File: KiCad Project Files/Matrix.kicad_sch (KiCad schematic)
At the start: 202 parts

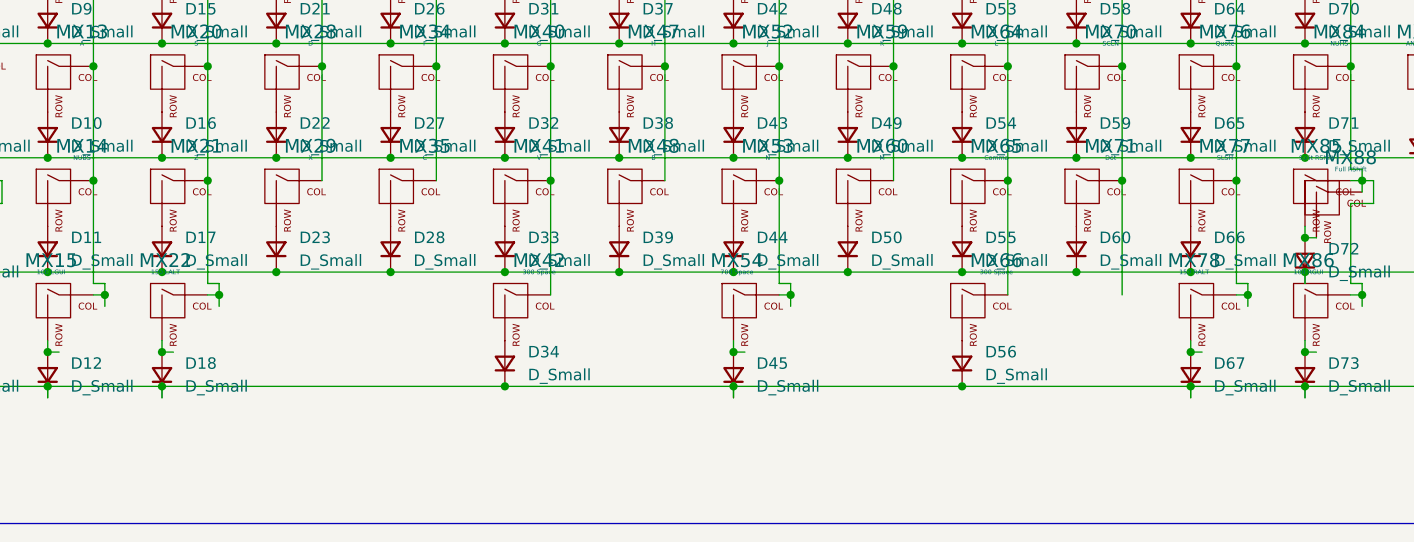
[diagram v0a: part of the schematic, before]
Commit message: added 225/275 support
2.75 stabs have break-away screw holes for compatibility with cases that need those areas of the PCB to be cut away
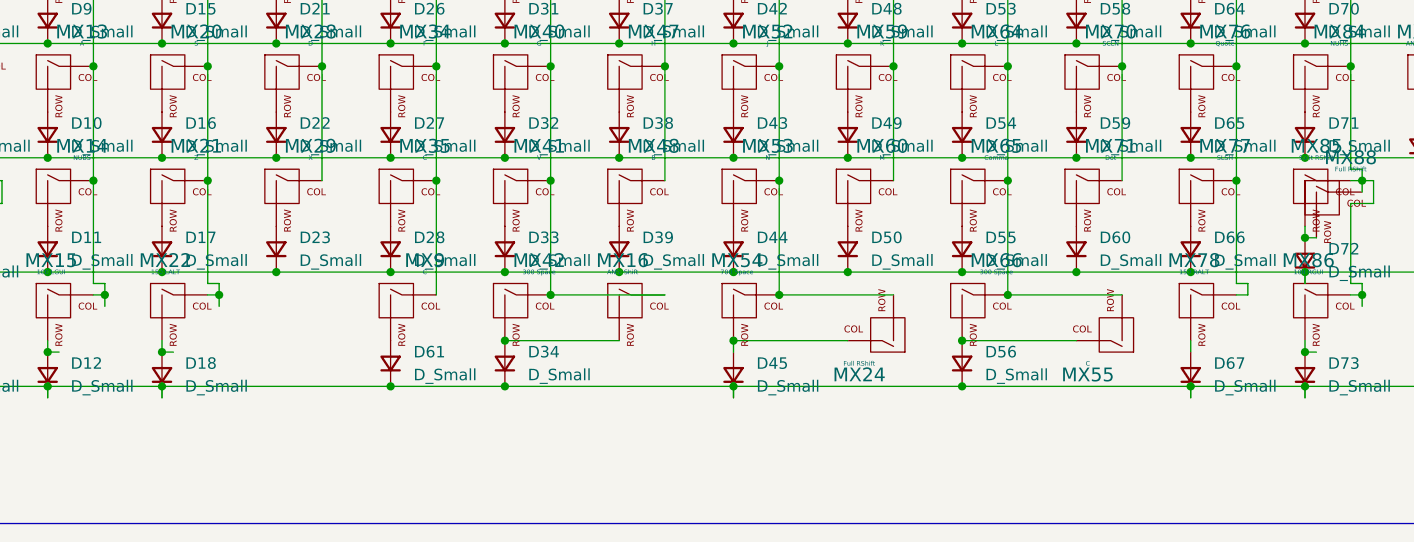
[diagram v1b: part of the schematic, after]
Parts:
- added D61: D_Small, Diode_SMD:D_SOD-123, symbol Device:D_Small
- added MX16: ANSI Shift, MX_Alps_Hybrid:MX-2.25U-NoLED, symbol cipulot_parts:MX-NoLED
- added MX24: Full RShift, MX_Alps_Hybrid:MX-2.75U-NoLED, symbol cipulot_parts:MX-NoLED
- added MX55, MX9: C, MX_Alps_Hybrid:MX-1U-NoLED, symbol cipulot_parts:MX-NoLED
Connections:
- net COL4: now also MX9.1 (COL)
- net COL5: now also MX16.1 (COL)
- net COL7: now also MX24.2 (ROW)
- net COL9: now also MX55.2 (ROW)
- net ROW5: now also D61.1 (K)
- net at D56.2 (A), MX66.2 (ROW): now also MX55.1 (COL)
- net at D45.2 (A), MX54.2 (ROW): now also MX24.1 (COL)
- net at D34.2 (A), MX42.2 (ROW): now also MX16.2 (ROW)
- new net: D61.2 (A), MX9.2 (ROW)
